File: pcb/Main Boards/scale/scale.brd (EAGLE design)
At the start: 65.1 x 51.2 mm, 29 parts, among them IC1 DS18B20+, J3 Spring Terminal, U1 NAU7802, X1 RJ45-8X

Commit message: Minor changes and cleanup
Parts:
- moved J3 11.6 mm to (-14.1, 18.4)
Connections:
- net A+: now also J3.3, J3.7
- net A-: now also J3.4, J3.8
- net GND: now also J3.2, J3.6
- net VDDA: now also J3.1, J3.5
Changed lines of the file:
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@@
 <attribute name="PROD_ID" value="RES-08380" x="27.355" y="6.105" size="1.778" layer="27" display="off"/>
 </element>
-<element name="J3" library="SparkFun-Connectors" package="1X04_SPRING_TERMINAL" value="Spring Terminal" x="-6.9" y="27.5" smashed="yes" rot="R90">
-<attribute name="NAME" x="-1.3" y="32.97" size="0.8128" layer="25" rot="R270" align="bottom-center"/>
-<attribute name="SF_ID" value="PRT-08075" x="60.2" y="27.5" size="1.778" layer="27" rot="R90" display="off"/>
+<element name="J3" library="SparkFun-Connectors" package="1X04_SPRING_TERMINAL" value="Spring Terminal" x="-14.1" y="18.4" smashed="yes" rot="R90">
+<attribute name="NAME" x="-8.5" y="23.87" size="0.8128" layer="25" rot="R270" align="bottom-center"/>
+<attribute name="SF_ID" value="PRT-08075" x="53" y="18.4" size="1.778" layer="27" rot="R90" display="off"/>
 </element>
 <element name="C5" library="Donnie" package="CAP_PTH-2.54" value="0.1μF" x="10.6" y="16" smashed="yes" rot="R180">
@@
 <wire x1="3.078" y1="34.078" x2="1.5" y2="34.078" width="1.016" layer="16"/>
 <wire x1="3.6" y1="34.6" x2="3.078" y2="34.078" width="1.016" layer="16"/>
+<contactref element="J3" pad="6"/>
+<contactref element="J3" pad="2"/>
+<wire x1="-16.64" y1="23.48" x2="-11.56" y2="23.48" width="0" layer="19" extent="1-1"/>
+<wire x1="1.5" y1="34.078" x2="-11.56" y2="23.48" width="0" layer="19" extent="1-1"/>
 </signal>
 <signal name="RDAT">
@@
 <wire x1="1.512" y1="36.86" x2="1.5" y2="36.872" width="0.4064" layer="1"/>
 <wire x1="1.5" y1="36.872" x2="1.5" y2="39.703" width="1.016" layer="1"/>
+<contactref element="J3" pad="1"/>
+<contactref element="J3" pad="5"/>
+<wire x1="-11.56" y1="26.02" x2="1.5" y2="36.872" width="0" layer="19" extent="1-1"/>
+<wire x1="-16.64" y1="26.02" x2="-11.56" y2="26.02" width="0" layer="19" extent="1-1"/>
 </signal>
 <signal name="N$11">
@@
 <signal name="A-">
 <contactref element="R6" pad="P$1"/>
+<contactref element="J3" pad="4"/>
+<contactref element="J3" pad="8"/>
+<wire x1="-11.56" y1="18.4" x2="12.005" y2="5.845" width="0" layer="19" extent="1-1"/>
+<wire x1="-16.64" y1="18.4" x2="-11.56" y2="18.4" width="0" layer="19" extent="1-1"/>
 </signal>
 <signal name="A+">
 <contactref element="R7" pad="P$1"/>
+<contactref element="J3" pad="3"/>
+<contactref element="J3" pad="7"/>
+<wire x1="-11.56" y1="20.94" x2="9.2" y2="5.845" width="0" layer="19" extent="1-1"/>
+<wire x1="-16.64" y1="20.94" x2="-11.56" y2="20.94" width="0" layer="19" extent="1-1"/>
 </signal>
 <signal name="N$1">

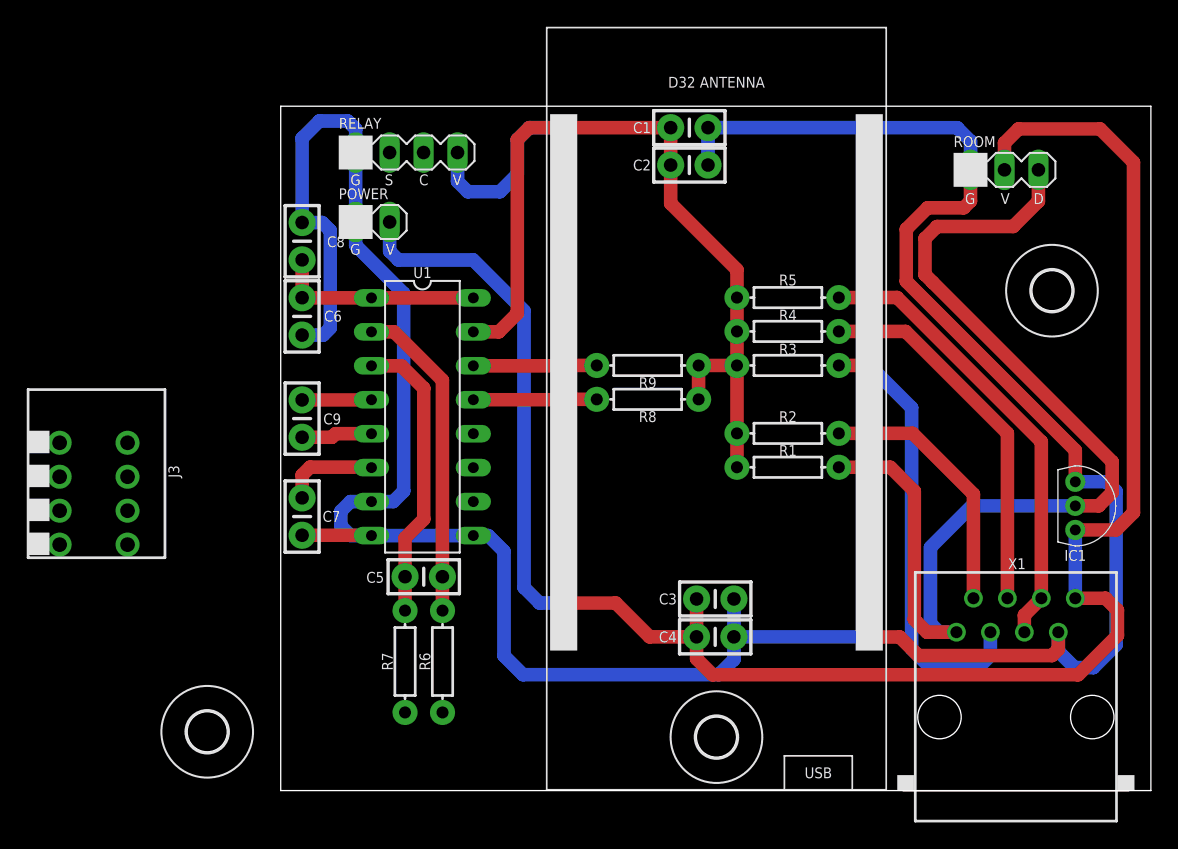
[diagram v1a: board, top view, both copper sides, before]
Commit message: Add scale terminal
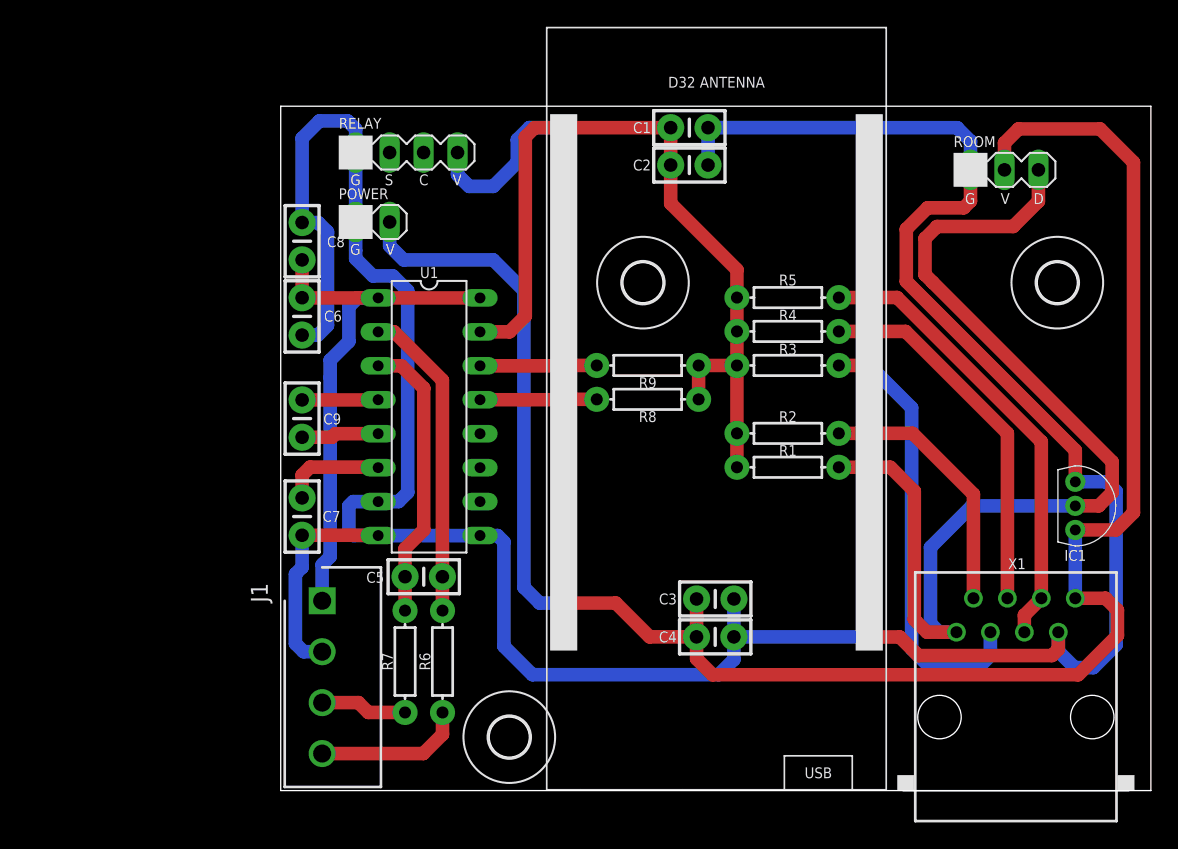
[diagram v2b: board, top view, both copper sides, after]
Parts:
- removed J3: Spring Terminal, SparkFun-Connectors:1X04_SPRING_TERMINAL
- added J1: 691321300004, SamacSys_Parts:SHDR4W80P0X381_1X4_1643X720X92
- moved U$3 34.4 mm to (27.0, 38.0)
- moved U$2 22.6 mm to (17.0, 4.00)
- moved U$1 0.72 mm to (58.0, 38.0)
- moved U1 0.50 mm to (11.0, 28.0)
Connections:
- net A+: now also J1.3; no longer J3.3, J3.7
- net A-: now also J1.4; no longer J3.4, J3.8
- net GND: now also J1.2; no longer J3.2, J3.6
- net VDDA: now also J1.1; no longer J3.1, J3.5
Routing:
- net VDDA: track 15.6 -> 41.4 mm
- net A-: track 0.00 -> 11.2 mm
- net GND: track 212.1 -> 223.3 mm
- net A+: track 0.00 -> 6.50 mm
- net 3V3: track 75.5 -> 74.1 mm
- net 5V: track 141.7 -> 142.3 mm
- net SDA: track 9.25 -> 8.75 mm
- net SCL: track 9.25 -> 8.75 mm
- net N$16: track 24.0 -> 23.5 mm
- net N$15: track 21.8 -> 21.3 mm
- net N$11: track 7.16 -> 7.66 mm
- net N$1: track 5.20 -> 5.70 mm
- net B+: track 5.30 -> 5.80 mm
